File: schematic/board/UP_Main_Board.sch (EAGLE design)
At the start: 18 parts

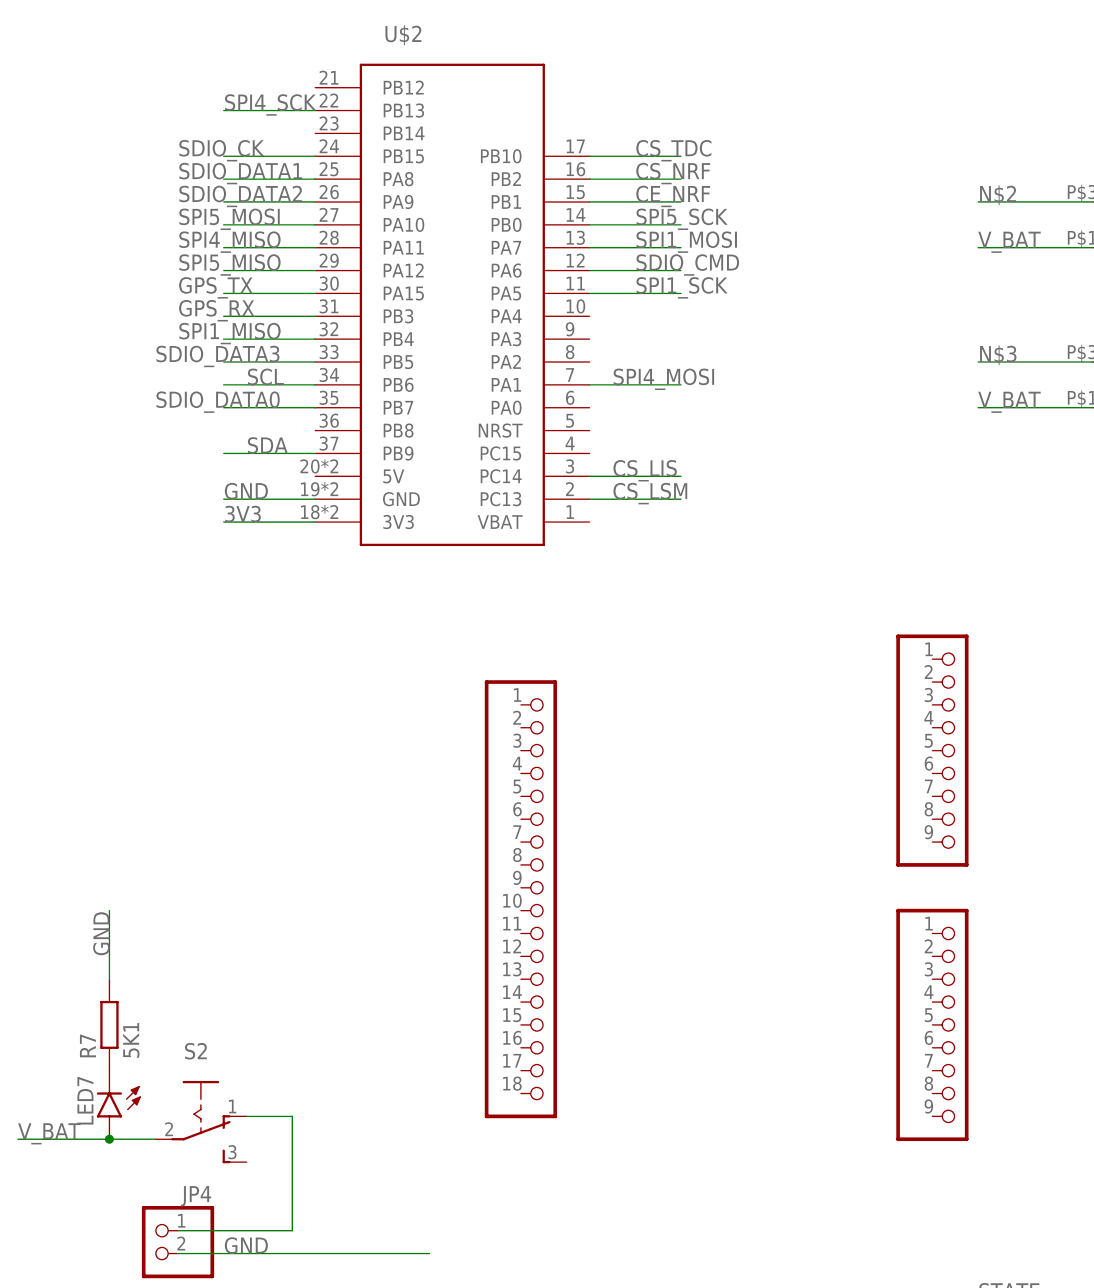
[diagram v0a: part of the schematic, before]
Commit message: 100501 раз изменил пины на плате
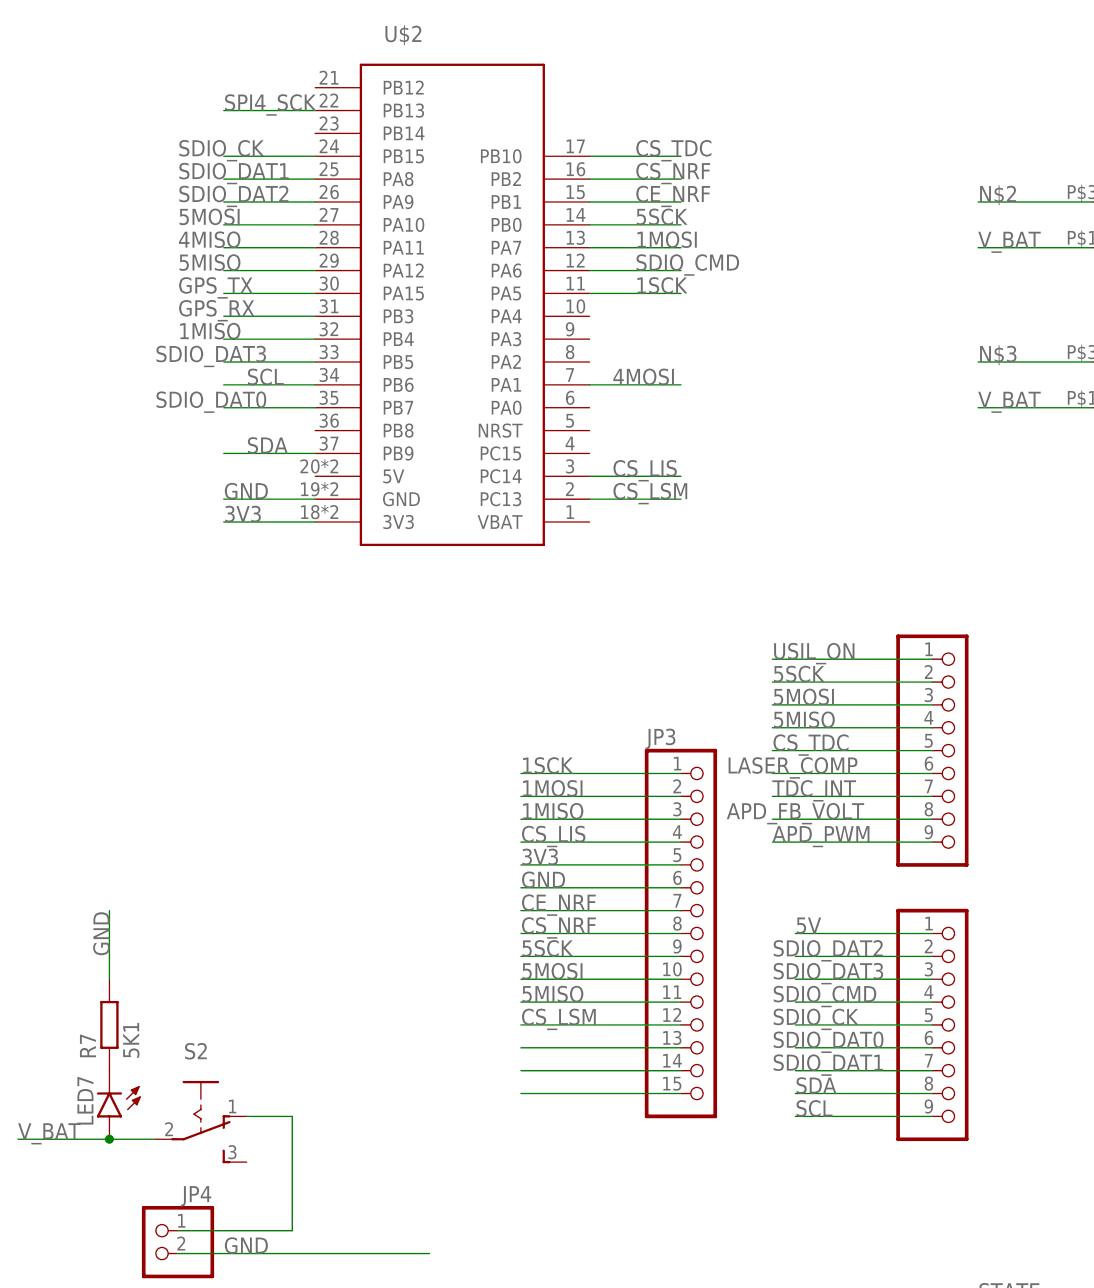
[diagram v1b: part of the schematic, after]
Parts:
- JP3: device pinhead:PINHD-1X18 -> pinhead:PINHD-1X15
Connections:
- net SPI4_MISO renamed 4MISO
- net SPI4_MOSI renamed 4MOSI
- removed net SDIO_DATA0: U$2.PB7
- removed net SDIO_DATA1: U$2.PA8
- removed net SDIO_DATA2: U$2.PA9
- removed net SDIO_DATA3: U$2.PB5
- removed net SPI1_MISO: U$2.PB4
- removed net SPI1_MOSI: U$2.PA7
- removed net SPI1_SCK: U$2.PA5
- removed net SPI5_MISO: U$2.PA12
- removed net SPI5_MOSI: U$2.PA10
- removed net SPI5_SCK: U$2.PB0
- new net 1MISO: JP3.3, U$2.PB4
- new net 1MOSI: JP3.2, U$2.PA7
- new net 1SCK: JP3.1, U$2.PA5
- new net 5MISO: JP1.4, JP3.11, U$2.PA12
- new net 5MOSI: JP1.3, JP3.10, U$2.PA10
- new net 5SCK: JP1.2, JP3.9, U$2.PB0
- new net APD_FB_VOLT: JP1.8
- new net APD_PWM: JP1.9
- new net LASER_COMP: JP1.6
- new net N$19: JP3.13
- new net N$20: JP3.14
- new net N$21: JP3.15
- new net SDIO_DAT0: JP2.6, U$2.PB7
- new net SDIO_DAT1: JP2.7, U$2.PA8
- new net SDIO_DAT2: JP2.2, U$2.PA9
- new net SDIO_DAT3: JP2.3, U$2.PB5
- new net TDC_INT: JP1.7
- new net USIL_ON: JP1.1
- net 3V3: now also JP3.5
- net 5V: now also JP2.1
- net CE_NRF: now also JP3.7
- net CS_LIS: now also JP3.4
- net CS_LSM: now also JP3.12
- net CS_NRF: now also JP3.8
- net CS_TDC: now also JP1.5
- net GND: now also JP3.6
- net SCL: now also JP2.9
- net SDA: now also JP2.8
- net SDIO_CK: now also JP2.5
- net SDIO_CMD: now also JP2.4

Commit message: Развод на плате...
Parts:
- U$3: device NEON-BLADE-2024:GPS_NEO7M_W-PPS -> NEON-BLADE-2023:GPS_NEO7M_W-PPS
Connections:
- removed net N$2: DC-DC_5V.IN-
- removed net N$3: DC-DC_3V3.IN-
- removed net SPI4_SCK: U$2.PB13
- new net 4SCK: JP1.2, U$2.PB13
- net 4MISO: now also JP1.4
- net 4MOSI: now also JP1.3
- net 5MISO: no longer JP1.4
- net 5MOSI: no longer JP1.3
- net 5SCK: no longer JP1.2
- net GND: now also DC-DC_3V3.IN-, DC-DC_5V.IN-
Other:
- moved on the sheet: U$3

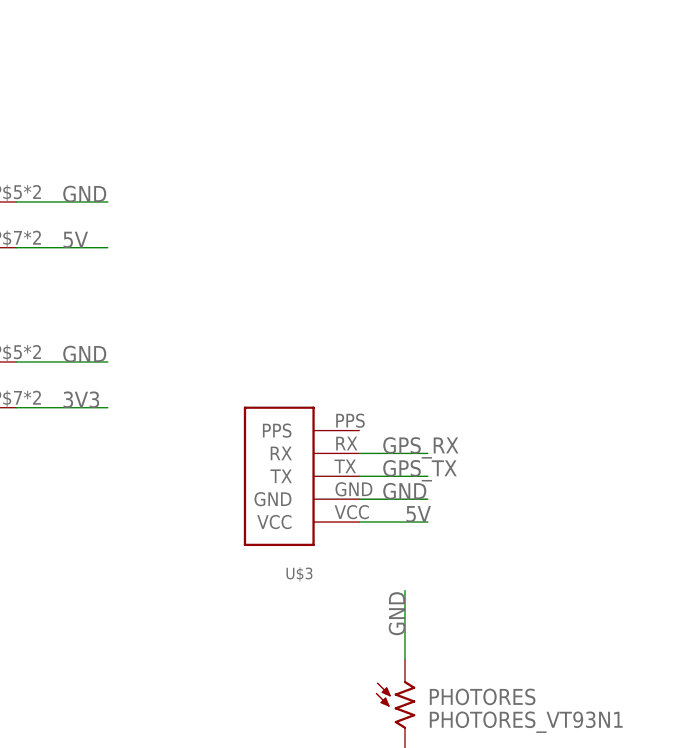
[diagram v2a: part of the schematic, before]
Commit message: поменял гпс на верхней плате
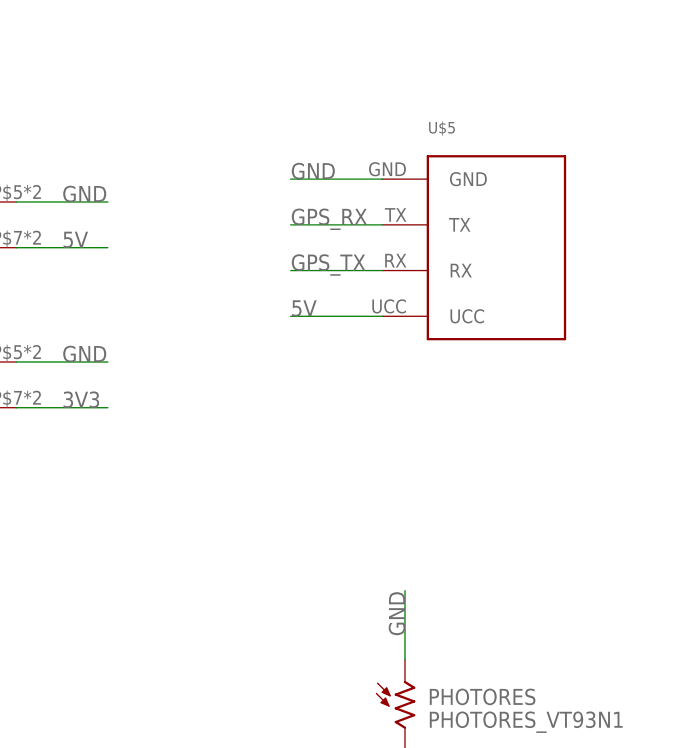
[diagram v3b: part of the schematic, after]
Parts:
- removed U$3: GPS_NEO7M_W-PPS, NEON-BLADE-2023:GPS_NEO7M_W-PPS
- added U$5: GPS, cansat-lib:GPS
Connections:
- net 5V: now also U$5.UCC; no longer U$3.VCC
- net GND: now also U$5.GND; no longer U$3.GND
- net GPS_RX: now also U$5.TX; no longer U$3.RX
- net GPS_TX: now also U$5.RX; no longer U$3.TX
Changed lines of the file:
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@@
 <part name="JP1" library="pinhead" library_urn="urn:adsk.eagle:library:325" deviceset="PINHD-1X9" device="" package3d_urn="urn:adsk.eagle:package:22483/2"/>
 <part name="JP3" library="pinhead" library_urn="urn:adsk.eagle:library:325" deviceset="PINHD-1X15" device="" package3d_urn="urn:adsk.eagle:package:22424/2"/>
-<part name="U$3" library="NEON-BLADE-2023" deviceset="GPS_NEO7M_W-PPS" device=""/>
+<part name="U$5" library="cansat-lib" deviceset="GPS" device=""/>
 </parts>
 <sheets>
@@
 <attribute name="VALUE" x="100.33" y="30.48" size="1.778" layer="96"/>
 </instance>
-<instance part="U$3" gate="G$1" x="205.74" y="104.14" smashed="yes" rot="R180">
-<attribute name="NAME" x="208.28" y="93.98" size="1.27" layer="95" rot="R180"/>
+<instance part="U$5" gate="G$1" x="228.6" y="129.54" smashed="yes">
+<attribute name="NAME" x="220.98" y="142.24" size="1.27" layer="95"/>
 </instance>
 </instances>
@@
 </segment>
 <segment>
-<wire x1="213.36" y1="101.6" x2="220.98" y2="101.6" width="0.1524" layer="91"/>
-<label x="215.9" y="101.6" size="1.778" layer="95"/>
-<pinref part="U$3" gate="G$1" pin="GND"/>
+<pinref part="U$5" gate="G$1" pin="GND"/>
+<wire x1="215.9" y1="137.16" x2="205.74" y2="137.16" width="0.1524" layer="91"/>
+<label x="205.74" y="137.16" size="1.778" layer="95"/>
 </segment>
 </net>
@@
 </segment>
 <segment>
-<wire x1="220.98" y1="99.06" x2="213.36" y2="99.06" width="0.1524" layer="91"/>
-<label x="218.44" y="99.06" size="1.778" layer="95"/>
-<pinref part="U$3" gate="G$1" pin="VCC"/>
+<pinref part="U$5" gate="G$1" pin="UCC"/>
+<wire x1="215.9" y1="121.92" x2="205.74" y2="121.92" width="0.1524" layer="91"/>
+<label x="205.74" y="121.92" size="1.778" layer="95"/>
 </segment>
 </net>
@@
 </segment>
 <segment>
-<wire x1="213.36" y1="104.14" x2="220.98" y2="104.14" width="0.1524" layer="91"/>
-<label x="215.9" y="104.14" size="1.778" layer="95"/>
-<pinref part="U$3" gate="G$1" pin="TX"/>
+<pinref part="U$5" gate="G$1" pin="RX"/>
+<wire x1="215.9" y1="127" x2="205.74" y2="127" width="0.1524" layer="91"/>
+<label x="205.74" y="127" size="1.778" layer="95"/>
 </segment>
 </net>
@@
 </segment>
 <segment>
-<wire x1="213.36" y1="106.68" x2="220.98" y2="106.68" width="0.1524" layer="91"/>
-<label x="215.9" y="106.68" size="1.778" layer="95"/>
-<pinref part="U$3" gate="G$1" pin="RX"/>
-</segment>
-</net>
+<pinref part="U$5" gate="G$1" pin="TX"/>
+<wire x1="215.9" y1="132.08" x2="205.74" y2="132.08" width="0.1524" layer="91"/>
+<label x="205.74" y="132.08" size="1.778" layer="95"/>
+</segment>
+</net>

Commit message: спонсор страданий
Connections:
- removed net N$20: JP3.14
- net V_BAT: now also JP3.14
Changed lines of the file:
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@@
 <pinref part="LED7" gate="G$1" pin="A"/>
+</segment>
+<segment>
+<pinref part="JP3" gate="A" pin="14"/>
+<wire x1="104.14" y1="38.1" x2="86.36" y2="38.1" width="0.1524" layer="91"/>
+<label x="86.36" y="38.1" size="1.778" layer="95"/>
 </segment>
 </net>
@@
 </segment>
 </net>
-<net name="N$20" class="0">
-<segment>
-<pinref part="JP3" gate="A" pin="14"/>
-<wire x1="104.14" y1="38.1" x2="86.36" y2="38.1" width="0.1524" layer="91"/>
-</segment>
-</net>

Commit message: почти добавил новый разъём
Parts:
- removed JP1, JP2: (no value), pinhead:PINHD-1X9
- removed JP3: (no value), pinhead:PINHD-1X15
- added U$6, U$7: PBS_SMD_X9, NEON-BLADE-2024:PBS_SMD_X9
- added U$8: PBS_SMD_X15, NEON-BLADE-2024:PBS_SMD_X15
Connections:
- removed net N$19: JP3.13
- removed net N$21: JP3.15
- new net N$2: U$8.13
- new net N$3: U$8.15
- net 1MISO: now also U$8.3; no longer JP3.3
- net 1MOSI: now also U$8.2; no longer JP3.2
- net 1SCK: now also U$8.1; no longer JP3.1
- net 3V3: now also U$8.5; no longer JP3.5
- net 4MISO: now also U$6.4; no longer JP1.4
- net 4MOSI: now also U$6.3; no longer JP1.3
- net 4SCK: now also U$6.2; no longer JP1.2
- net 5MISO: now also U$8.11; no longer JP3.11
- net 5MOSI: now also U$8.10; no longer JP3.10
- net 5SCK: now also U$8.9; no longer JP3.9
- net 5V: now also U$7.1; no longer JP2.1
- net APD_FB_VOLT: now also U$6.8; no longer JP1.8
- net APD_PWM: now also U$6.9; no longer JP1.9
- net CE_NRF: now also U$8.7; no longer JP3.7
- net CS_LIS: now also U$8.4; no longer JP3.4
- net CS_LSM: now also U$8.12; no longer JP3.12
- net CS_NRF: now also U$8.8; no longer JP3.8
- net CS_TDC: now also U$6.5; no longer JP1.5
- net GND: now also U$8.6; no longer JP3.6
- net LASER_COMP: now also U$6.6; no longer JP1.6
- net SCL: now also U$7.9; no longer JP2.9
- net SDA: now also U$7.8; no longer JP2.8
- net SDIO_CK: now also U$7.5; no longer JP2.5
- net SDIO_CMD: now also U$7.4; no longer JP2.4
- net SDIO_DAT0: now also U$7.6; no longer JP2.6
- net SDIO_DAT1: now also U$7.7; no longer JP2.7
- net SDIO_DAT2: now also U$7.2; no longer JP2.2
- net SDIO_DAT3: now also U$7.3; no longer JP2.3
- net TDC_INT: now also U$6.7; no longer JP1.7
- net USIL_ON: now also U$6.1; no longer JP1.1
- net V_BAT: now also U$8.14; no longer JP3.14

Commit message: переделки по плате
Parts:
- added JP1: (no value), pinhead:PINHD-1X2
- added R4: 2k, rcl:R-EU_R0603
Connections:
- net N$2 renamed COMP_DAC
- new net LED: R4.1, U$2.PB14
- new net N$37: JP1.2, R4.2
- net 3V3: now also JP1.1
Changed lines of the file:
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@@
 <part name="U$7" library="NEON-BLADE-2024" deviceset="PBS_SMD_X9" device=""/>
 <part name="U$8" library="NEON-BLADE-2024" deviceset="PBS_SMD_X15" device=""/>
+<part name="R4" library="rcl" library_urn="urn:adsk.eagle:library:334" deviceset="R-EU_" device="R0603" package3d_urn="urn:adsk.eagle:package:23555/3" value="2k"/>
+<part name="JP1" library="pinhead" library_urn="urn:adsk.eagle:library:325" deviceset="PINHD-1X2" device="" package3d_urn="urn:adsk.eagle:package:22435/2"/>
 </parts>
 <sheets>
@@
 <attribute name="VALUE" x="100.33" y="-48.26" size="1.778" layer="96"/>
 </instance>
+<instance part="R4" gate="G$1" x="12.7" y="142.24" smashed="yes">
+<attribute name="NAME" x="8.89" y="143.7386" size="1.778" layer="95"/>
+<attribute name="VALUE" x="8.89" y="138.938" size="1.778" layer="96"/>
+</instance>
+<instance part="JP1" gate="G$1" x="25.4" y="142.24" smashed="yes">
+<attribute name="NAME" x="19.05" y="147.955" size="1.778" layer="95"/>
+<attribute name="VALUE" x="19.05" y="137.16" size="1.778" layer="96"/>
+</instance>
 </instances>
 <busses>
@@
 <label x="86.36" y="-17.78" size="1.778" layer="95"/>
 <pinref part="U$8" gate="G$1" pin="5"/>
+</segment>
+<segment>
+<pinref part="JP1" gate="G$1" pin="1"/>
+<wire x1="22.86" y1="144.78" x2="12.7" y2="144.78" width="0.1524" layer="91"/>
+<label x="12.7" y="144.78" size="1.778" layer="95"/>
 </segment>
 </net>
@@
 </segment>
 </net>
-<net name="N$2" class="0">
+<net name="COMP_DAC" class="0">
 <segment>
 <wire x1="104.14" y1="-38.1" x2="86.36" y2="-38.1" width="0.1524" layer="91"/>
 <pinref part="U$8" gate="G$1" pin="13"/>
+<label x="86.36" y="-38.1" size="1.778" layer="95"/>
 </segment>
 </net>
@@
 </segment>
 </net>
+<net name="LED" class="0">
+<segment>
+<pinref part="U$2" gate="G$1" pin="PB14"/>
+<wire x1="63.5" y1="142.24" x2="53.34" y2="142.24" width="0.1524" layer="91"/>
+<label x="55.88" y="142.24" size="1.778" layer="95"/>
+</segment>
+<segment>
+<pinref part="R4" gate="G$1" pin="1"/>
+<wire x1="7.62" y1="142.24" x2="2.54" y2="142.24" width="0.1524" layer="91"/>
+<label x="3.048" y="143.002" size="1.778" layer="95"/>
+</segment>
+</net>
+<net name="N$37" class="0">
+<segment>
+<pinref part="R4" gate="G$1" pin="2"/>
+<wire x1="22.86" y1="142.24" x2="17.78" y2="142.24" width="0.1524" layer="91"/>
+<pinref part="JP1" gate="G$1" pin="2"/>
+</segment>
+</net>

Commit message: ПЕРЕДЕЛАЙ ПАЛТЫ
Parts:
- removed 3V3, 5V: (no value), NEON-BLADE-2023:VIAS-CONNECT
- R17: value 191k/2k -> 2k
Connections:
- removed net N$13: 3V3.2, 5V.1, R17.1
- net 3V3: now also R17.1; no longer 3V3.1
- net 5V: no longer 5V.2
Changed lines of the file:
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@@
 <part name="DC-DC_3V3" library="NEON-BLADE-2023" deviceset="MP1584-B" device=""/>
 <part name="PHOTORES" library="NEON-BLADE-2023" deviceset="PHOTORES_VT93N1" device=""/>
-<part name="R17" library="rcl" library_urn="urn:adsk.eagle:library:334" deviceset="R-EU_" device="R0603" package3d_urn="urn:adsk.eagle:package:23555/3" value="191k/2k"/>
-<part name="3V3" library="NEON-BLADE-2023" deviceset="VIAS-CONNECT" device=""/>
-<part name="5V" library="NEON-BLADE-2023" deviceset="VIAS-CONNECT" device=""/>
+<part name="R17" library="rcl" library_urn="urn:adsk.eagle:library:334" deviceset="R-EU_" device="R0603" package3d_urn="urn:adsk.eagle:package:23555/3" value="2k"/>
 <part name="U$10" library="NEON-BLADE-2023" deviceset="MSS12D01" device=""/>
 <part name="R8" library="rcl" library_urn="urn:adsk.eagle:library:334" deviceset="R-EU_" device="R0603" package3d_urn="urn:adsk.eagle:package:23555/3" value="2k"/>
@@
 <attribute name="VALUE" x="221.742" y="59.69" size="1.778" layer="96" rot="R90"/>
 </instance>
-<instance part="3V3" gate="G$1" x="213.36" y="50.8" smashed="yes">
-<attribute name="NAME" x="212.09" y="53.975" size="1.778" layer="95"/>
-<attribute name="VALUE" x="209.55" y="46.355" size="1.778" layer="96"/>
-</instance>
-<instance part="5V" gate="G$1" x="223.52" y="50.8" smashed="yes">
-<attribute name="NAME" x="222.25" y="53.975" size="1.778" layer="95"/>
-<attribute name="VALUE" x="219.71" y="46.355" size="1.778" layer="96"/>
-</instance>
 <instance part="U$10" gate="G$1" x="172.72" y="15.24" smashed="yes" rot="R270">
 <attribute name="NAME" x="170.815" y="21.59" size="1.778" layer="95"/>
@@
 </segment>
 <segment>
-<wire x1="210.82" y1="50.8" x2="203.2" y2="50.8" width="0.1524" layer="91"/>
-<label x="203.2" y="50.8" size="1.778" layer="95"/>
-<pinref part="3V3" gate="G$1" pin="1"/>
-</segment>
-<segment>
 <wire x1="177.8" y1="10.16" x2="187.96" y2="10.16" width="0.1524" layer="91"/>
 <label x="185.42" y="10.16" size="1.778" layer="95"/>
@@
 <label x="12.7" y="144.78" size="1.778" layer="95"/>
 </segment>
+<segment>
+<wire x1="218.44" y1="58.42" x2="218.44" y2="50.8" width="0.1524" layer="91"/>
+<pinref part="R17" gate="G$1" pin="1"/>
+<label x="215.9" y="50.8" size="1.778" layer="95"/>
+</segment>
 </net>
 <net name="5V" class="0">
@@
 <label x="180.34" y="129.54" size="1.778" layer="95"/>
 <pinref part="DC-DC_5V" gate="G$1" pin="OUT+"/>
-</segment>
-<segment>
-<wire x1="226.06" y1="50.8" x2="236.22" y2="50.8" width="0.1524" layer="91"/>
-<label x="233.68" y="50.8" size="1.778" layer="95"/>
-<pinref part="5V" gate="G$1" pin="2"/>
 </segment>
 <segment>
@@
 </segment>
 </net>
-<net name="N$13" class="0">
-<segment>
-<wire x1="218.44" y1="58.42" x2="218.44" y2="50.8" width="0.1524" layer="91"/>
-<wire x1="218.44" y1="50.8" x2="215.9" y2="50.8" width="0.1524" layer="91"/>
-<wire x1="220.98" y1="50.8" x2="218.44" y2="50.8" width="0.1524" layer="91"/>
-<junction x="218.44" y="50.8"/>
-<pinref part="R17" gate="G$1" pin="1"/>
-<pinref part="3V3" gate="G$1" pin="2"/>
-<pinref part="5V" gate="G$1" pin="1"/>
-</segment>
-</net>

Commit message: чипи чипи чапа чапа дуби дуби
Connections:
- removed net APD_FB_VOLT: U$6.8
- removed net APD_PWM: U$6.9
- removed net COMP_DAC: U$8.13
- removed net LASER_COMP: U$6.6
- removed net N$3: U$8.15
- net USIL_ON: now also U$2.PA0
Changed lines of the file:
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@@
 <pinref part="U$6" gate="G$1" pin="1"/>
 </segment>
-</net>
-<net name="LASER_COMP" class="0">
 <segment>
-<wire x1="132.08" y1="-7.62" x2="114.3" y2="-7.62" width="0.1524" layer="91"/>
-<label x="109.22" y="-7.62" size="1.778" layer="95"/>
-<pinref part="U$6" gate="G$1" pin="6"/>
+<pinref part="U$2" gate="G$1" pin="PA0"/>
+<wire x1="93.98" y1="111.76" x2="104.14" y2="111.76" width="0.1524" layer="91"/>
+<label x="96.52" y="111.76" size="1.778" layer="95"/>
 </segment>
 </net>
@@
 <label x="114.3" y="-10.16" size="1.778" layer="95"/>
 <pinref part="U$6" gate="G$1" pin="7"/>
-</segment>
-</net>
-<net name="APD_FB_VOLT" class="0">
-<segment>
-<wire x1="132.08" y1="-12.7" x2="114.3" y2="-12.7" width="0.1524" layer="91"/>
-<label x="109.22" y="-12.7" size="1.778" layer="95"/>
-<pinref part="U$6" gate="G$1" pin="8"/>
-</segment>
-</net>
-<net name="APD_PWM" class="0">
-<segment>
-<wire x1="132.08" y1="-15.24" x2="114.3" y2="-15.24" width="0.1524" layer="91"/>
-<label x="114.3" y="-15.24" size="1.778" layer="95"/>
-<pinref part="U$6" gate="G$1" pin="9"/>
 </segment>
 </net>
@@
 </segment>
 </net>
-<net name="COMP_DAC" class="0">
-<segment>
-<wire x1="104.14" y1="-38.1" x2="86.36" y2="-38.1" width="0.1524" layer="91"/>
-<pinref part="U$8" gate="G$1" pin="13"/>
-<label x="86.36" y="-38.1" size="1.778" layer="95"/>
-</segment>
-</net>
-<net name="N$3" class="0">
-<segment>
-<wire x1="104.14" y1="-43.18" x2="86.36" y2="-43.18" width="0.1524" layer="91"/>
-<pinref part="U$8" gate="G$1" pin="15"/>
-</segment>
-</net>
